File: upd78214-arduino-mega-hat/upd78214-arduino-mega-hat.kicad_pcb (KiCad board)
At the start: 4 copper layers, 101.6 x 53.3 mm, 17 parts, among them J1 Power, J2 PWM, J3 Analog, J4 PWM, J5 Analog, J6 Communication, J7 Digital, U1 upd78214-64p-qfp, Y1 4-12MHz

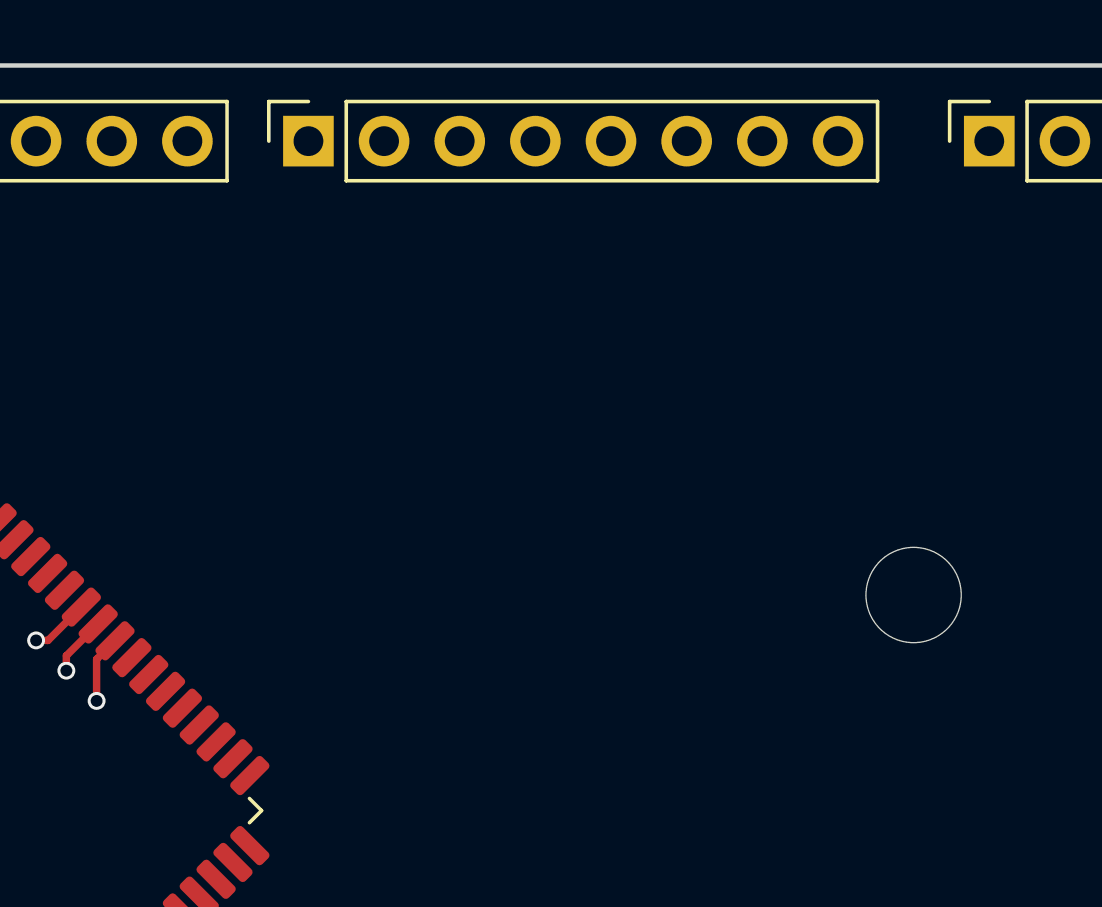
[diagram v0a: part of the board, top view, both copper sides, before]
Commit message: TX/RX jumpers, enormous memory products data book
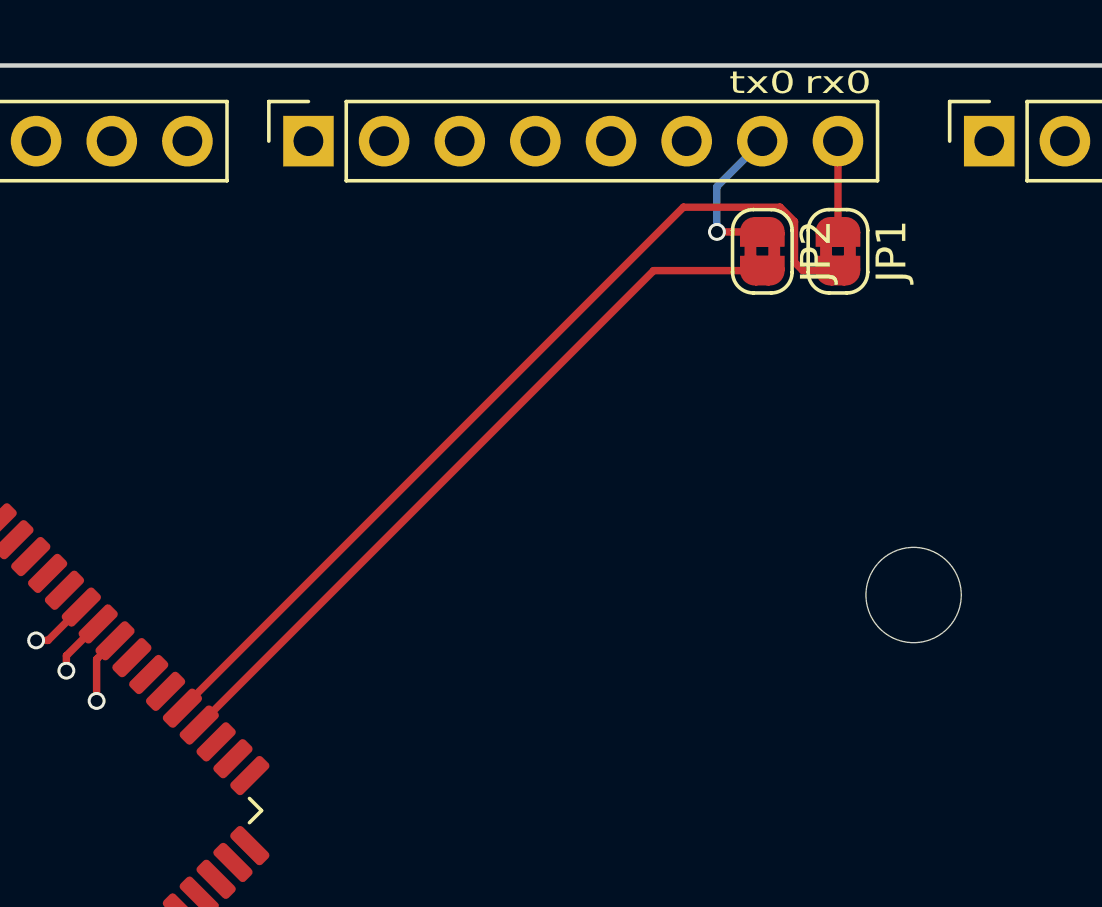
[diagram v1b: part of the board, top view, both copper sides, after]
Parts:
- added JP1: Jumper_2_Bridged, Jumper:SolderJumper-2_P1.3mm_Bridged2Bar_RoundedPad1.0x1.5mm, F.Cu at (163.5, 52.9)
- added JP2: Jumper_2_Bridged, Jumper:SolderJumper-2_P1.3mm_Bridged2Bar_RoundedPad1.0x1.5mm, F.Cu at (161.0, 52.9)
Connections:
- U1 pad 36: unconnected-(U1-p3,0/rxd-Pad36) -> Net-(JP2-B)
- U1 pad 37: unconnected-(U1-p3,1/txd-Pad37) -> Net-(JP1-B)
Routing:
- net Net-(JP1-B): track 0.00 -> 30.7 mm
- net Net-(JP2-B): track 0.00 -> 25.2 mm
- net /TX0/1: track 0.00 -> 5.20 mm, vias 0 -> 1
- net /RX0/0: track 0.00 -> 3.05 mm
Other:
- board text added: "rx0"
- board text added: "tx0"

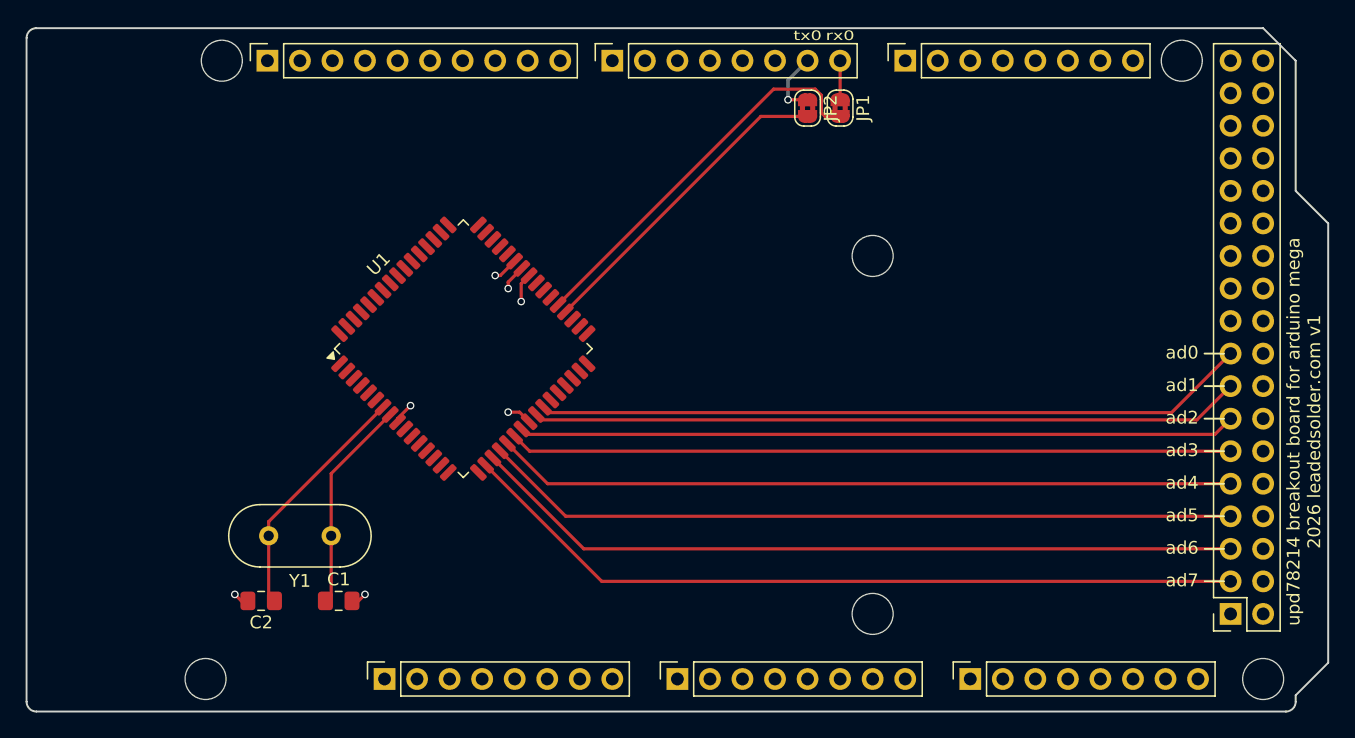
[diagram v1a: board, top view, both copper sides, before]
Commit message: Route a8..15
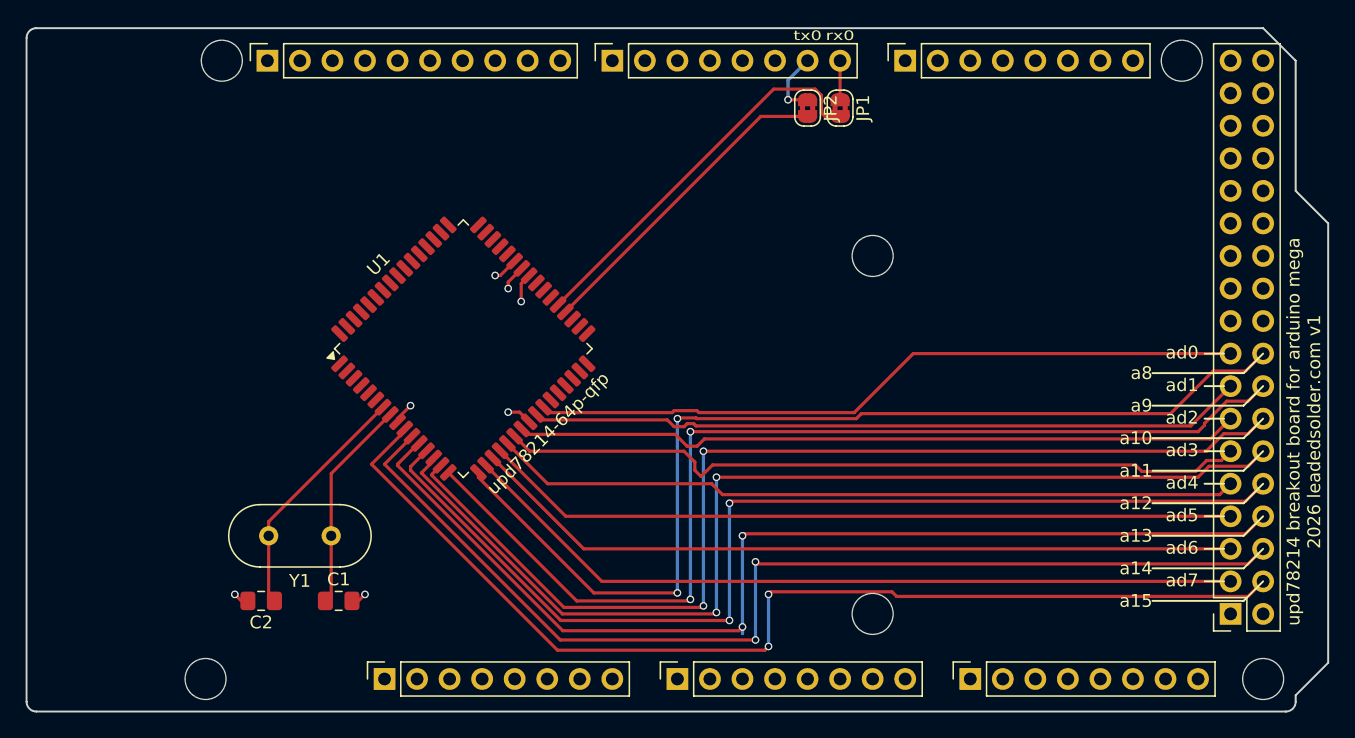
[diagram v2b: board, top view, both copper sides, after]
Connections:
- J7 pad 10: /47 -> /a12
- J7 pad 12: /*45 -> /a11
- J7 pad 14: /43 -> /a10
- J7 pad 16: /41 -> /a9
- J7 pad 18: /39 -> /a8
- J7 pad 4: /53 -> /a15
- J7 pad 6: /51 -> /a14
- J7 pad 8: /49 -> /a13
- U1 pad 10: unconnected-(U1-p5,7/a15-Pad10) -> /a15
- U1 pad 11: unconnected-(U1-p5,6/a14-Pad11) -> /a14
- U1 pad 12: unconnected-(U1-p5,5/a13-Pad12) -> /a13
- U1 pad 13: unconnected-(U1-p5,4/a12-Pad13) -> /a12
- U1 pad 14: unconnected-(U1-p5,3/a11-Pad14) -> /a11
- U1 pad 15: unconnected-(U1-p5,2/a10-Pad15) -> /a10
- U1 pad 16: unconnected-(U1-p5,1/a9-Pad16) -> /a9
- U1 pad 17: unconnected-(U1-p5,0/a8-Pad17) -> /a8
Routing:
- net /a15: track 0.00 -> 84.3 mm, vias 0 -> 2
- net /a13: track 0.00 -> 84.3 mm, vias 0 -> 2
- net /a14: track 0.00 -> 84.0 mm, vias 0 -> 2
- net /a10: track 0.00 -> 83.4 mm, vias 0 -> 2
- net /a11: track 0.00 -> 83.3 mm, vias 0 -> 2
- net /a12: track 0.00 -> 83.2 mm, vias 0 -> 2
- net /a9: track 0.00 -> 82.5 mm, vias 0 -> 2
- net /a8: track 0.00 -> 81.1 mm, vias 0 -> 2
- net /ad3: track 56.4 -> 58.8 mm
- net /ad2: track 56.0 -> 56.8 mm
- net /ad4: track 57.8 -> 58.5 mm
- net /ad1: track 55.5 -> 56.0 mm
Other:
- board text added: "a10"
- board text added: "a11"
- board text added: "a12"
- board text added: "a13"
- board text added: "a14"
- board text added: "a15"
- board text added: "a8"
- board text added: "a9"
